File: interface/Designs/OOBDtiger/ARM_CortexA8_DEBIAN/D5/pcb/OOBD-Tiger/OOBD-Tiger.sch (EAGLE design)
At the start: 122 parts, among them IC1 ADM3053M, IC2 ADM3053M, IC4 DS3231, U1 SY6280, U10 MP1482DS, U2 SN65HVD230(SO8), U3 SY6280, U6 SN65HVD230(SO8)

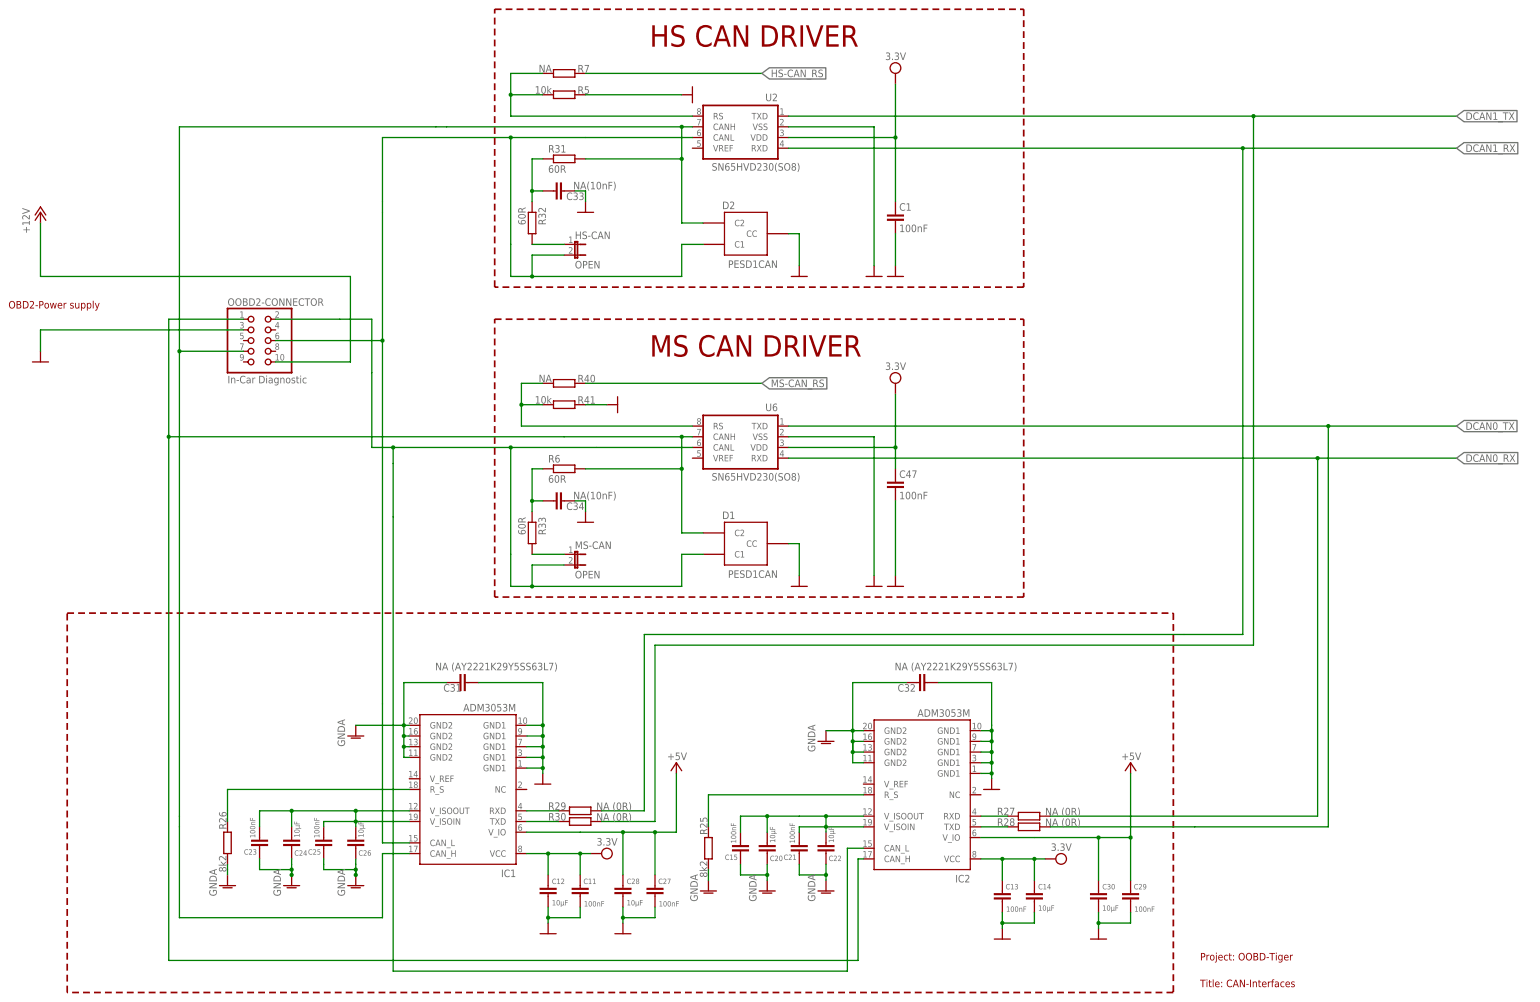
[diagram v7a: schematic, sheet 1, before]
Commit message: Letzter Stand, Endplaziert,Teilweise gerouted.
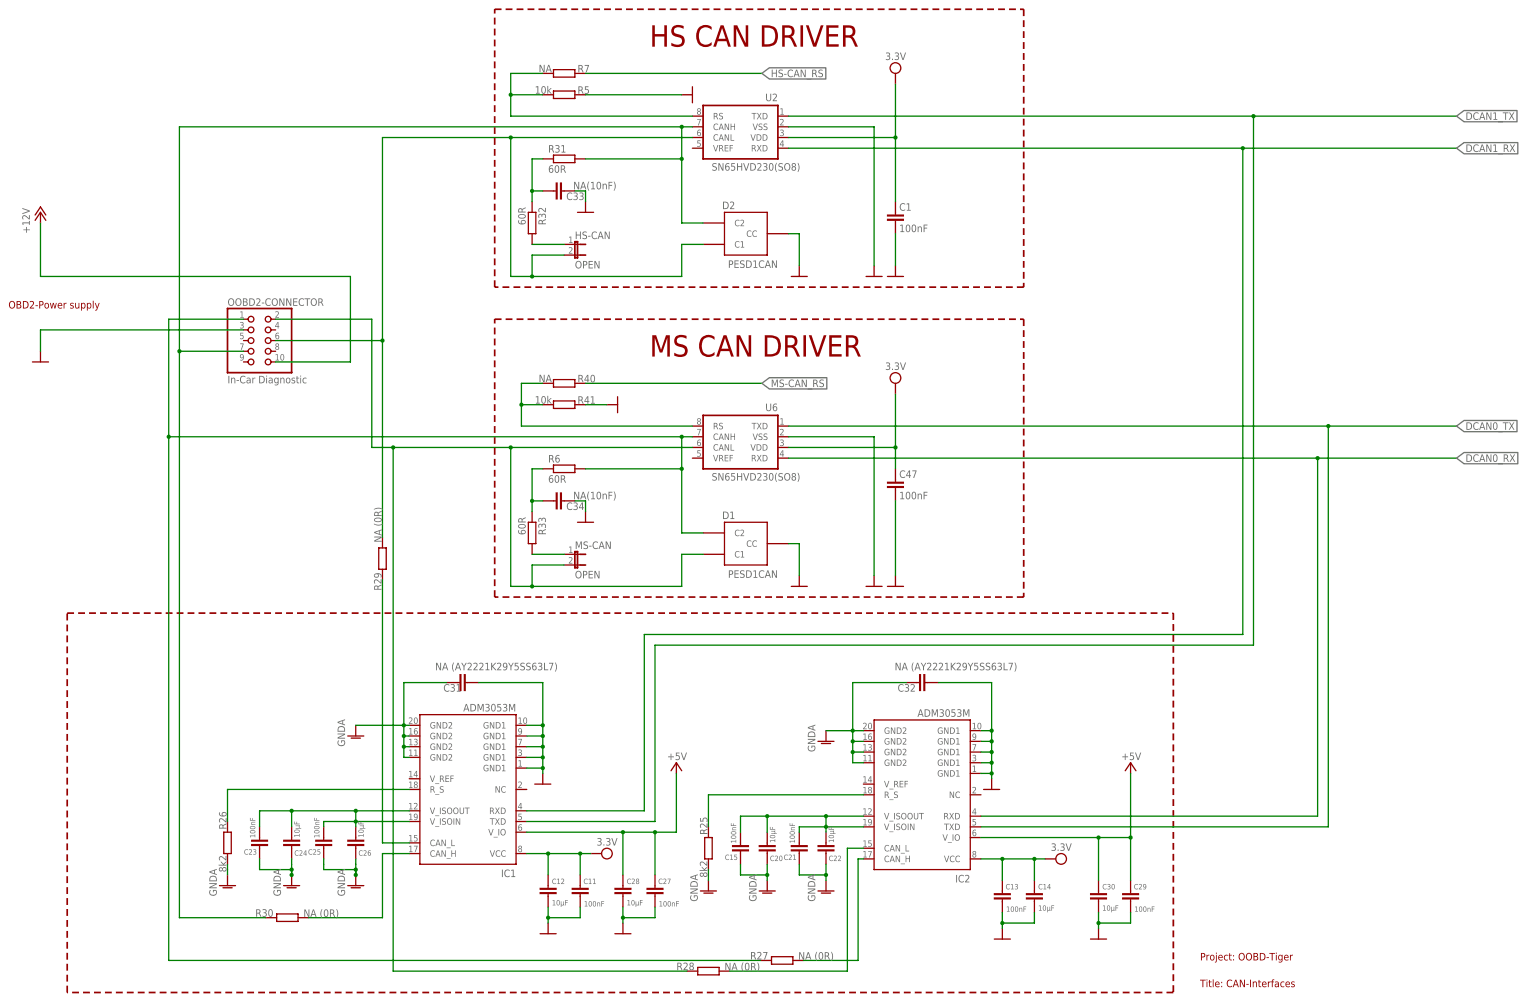
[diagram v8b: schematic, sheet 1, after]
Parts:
- C10, C14, C63, C64, C8: device rcl:C-EUC0805K -> rcl:C-EUC0603
- HS-CAN, MS-CAN: device SparkFun:JUMPER-2SMD-NO -> SparkFun:JUMPER-2PTH
- L5, L6: device rcl:L-USL0805_5MIL_DWS -> rcl:L-USL0603
- WAKE-UP: device SparkFun:JUMPER-2SMD-NO -> SparkFun:JUMPER-2PTH_LOCK
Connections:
- removed net N$39: IC1.RXD, R29.1
- removed net N$41: IC1.TXD, R30.1
- new net N$12: IC2.CAN_H, R27.2
- new net N$36: IC1.CAN_L, R29.1
- new net N$37: IC1.TXD
- new net N$38: IC1.RXD
- net CAN0_H: now also R27.1; no longer IC2.CAN_H
- net CAN0_L: now also R28.1; no longer IC2.CAN_L
- net CAN1_H: now also R30.1; no longer IC1.CAN_H
- net CAN1_L: now also R29.2; no longer IC1.CAN_L
- net DCAN0_RX: now also IC2.RXD; no longer R27.2
- net DCAN0_TX: now also IC2.TXD; no longer R28.2
- net DCAN1_RX: no longer R29.2
- net DCAN1_TX: no longer R30.2
- net N$34: now also IC2.CAN_L, R28.2; no longer IC2.RXD, R27.1
- net N$35: now also IC1.CAN_H, R30.2; no longer IC2.TXD, R28.1
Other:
- moved on the sheet: R27, R28, R29, R30
